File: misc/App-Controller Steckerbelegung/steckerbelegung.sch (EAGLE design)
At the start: 1 part

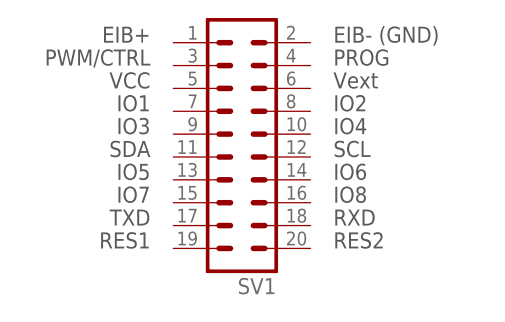
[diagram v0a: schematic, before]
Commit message: Pin Vext auf Versorgung korrigiert
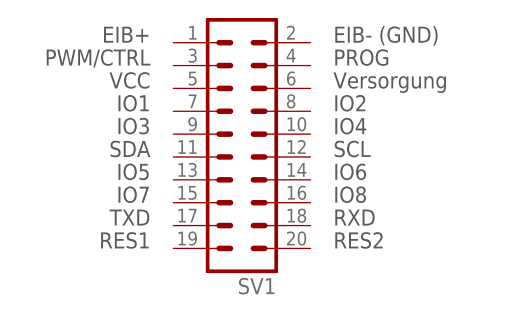
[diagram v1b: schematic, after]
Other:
- note added: "Versorgung"
- note removed: "Vext"
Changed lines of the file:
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@@
 <text x="60.96" y="50.8" size="1.778" layer="92">EIB- (GND)</text>
 <text x="60.96" y="48.26" size="1.778" layer="92">PROG</text>
-<text x="60.96" y="45.72" size="1.778" layer="92">Vext</text>
+<text x="60.96" y="45.72" size="1.778" layer="92">Versorgung</text>
 <text x="60.96" y="43.18" size="1.778" layer="92">IO2</text>
 <text x="60.96" y="40.64" size="1.778" layer="92">IO4</text>
